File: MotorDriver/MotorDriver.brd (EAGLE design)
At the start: 36.3 x 29.8 mm, 27 parts, among them U1 MCP4013, U2 DRV8848, U3 ATTINY841

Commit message: Various small tweaks based on testing and feedback from manufacturer.
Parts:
- added D2: RB751V40, Modulo:SOD-323
- R12, R13: value 150Ω -> 0Ω
- moved C1 8.64 mm to (9.21, 24.6)
- moved R12 1.59 mm to (11.3, 27.3)
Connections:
- new net N$2: D2.C, U1.1
- net VCC: now also D2.A; no longer U1.1
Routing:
- net VCC: track 52.3 -> 39.8 mm
- net N$2: track 0.00 -> 11.0 mm, vias 0 -> 1
- net GND: track 53.0 -> 51.3 mm
- net SCL: track 24.5 -> 25.9 mm
- net SCL/SCK: track 11.6 -> 12.7 mm
- net MISO/LED: track 20.7 -> 21.6 mm

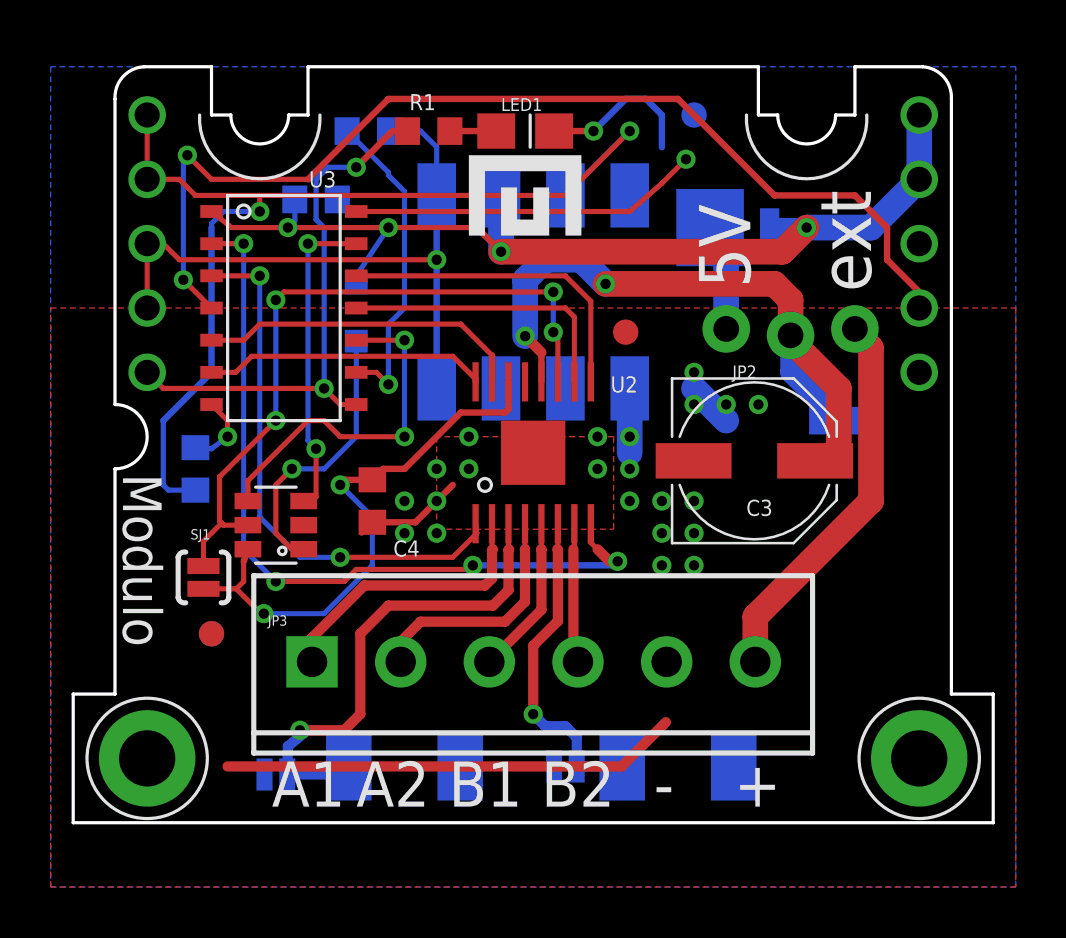
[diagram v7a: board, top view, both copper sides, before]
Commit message: Added unique board prefixes to part numbers due to CM requirements
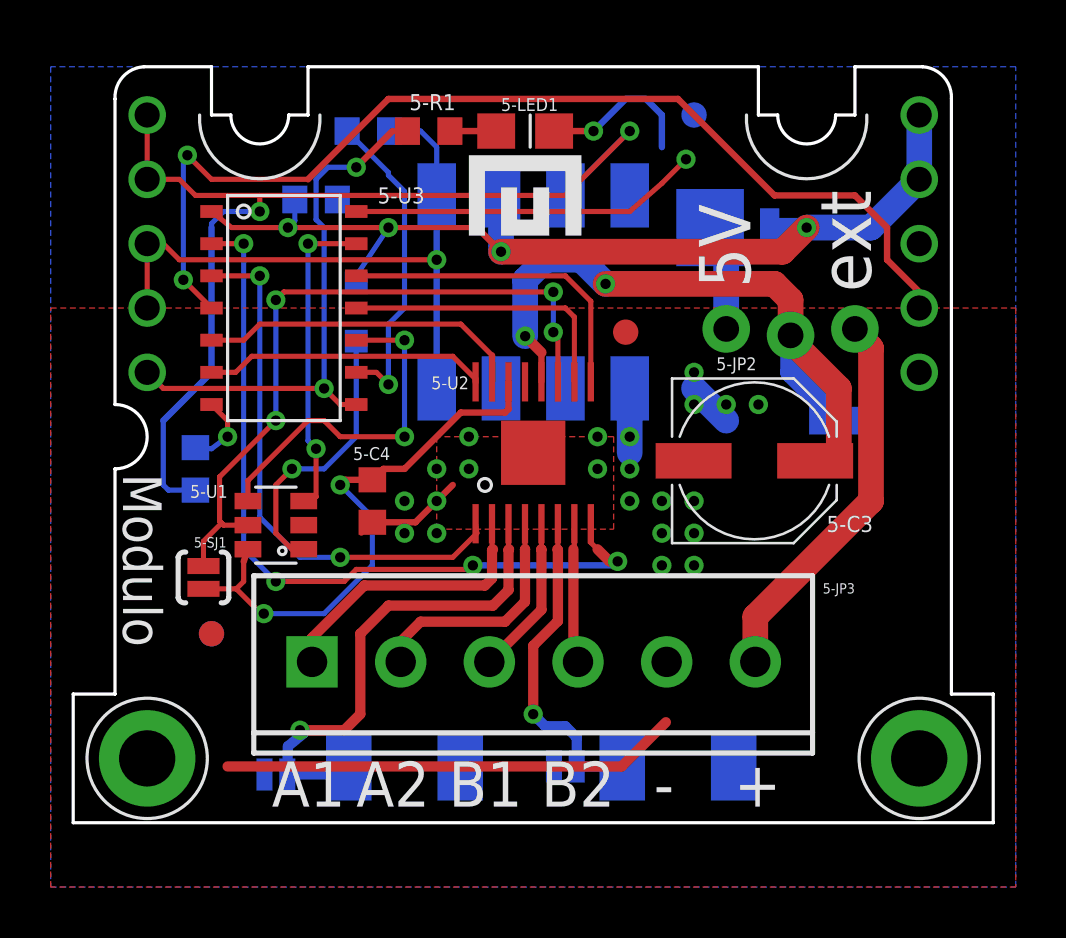
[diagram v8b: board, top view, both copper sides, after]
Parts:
- removed F2, F3: FIDUCIAL, Modulo:FIDUCIAL_1MM
- added 5-F2, 5-F3: FIDUCIAL, Modulo:FIDUCIAL_1MM
- renumbered C1 to 5-C1, C2 to 5-C2, C3 to 5-C3, C4 to 5-C4, D1 to 5-D1, D2 to 5-D2, F1 to 5-F1, F4 to 5-F4, JP1 to 5-JP1, JP2 to 5-JP2, JP3 to 5-JP3, LED1 to 5-LED1, PCB1 to 5-PCB1, R1 to 5-R1, R12 to 5-R12, R13 to 5-R13, R3 to 5-R3, R4 to 5-R4, SJ1 to 5-SJ1, SJ2 to 5-SJ2, SJ3 to 5-SJ3, U1 to 5-U1, U2 to 5-U2, U3 to 5-U3
